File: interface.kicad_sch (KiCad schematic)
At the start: 10 parts, among them J6 JST Header, Q3 DTC043Z, Q5 DTC043Z, SW2 RotaryEncoder_Switch

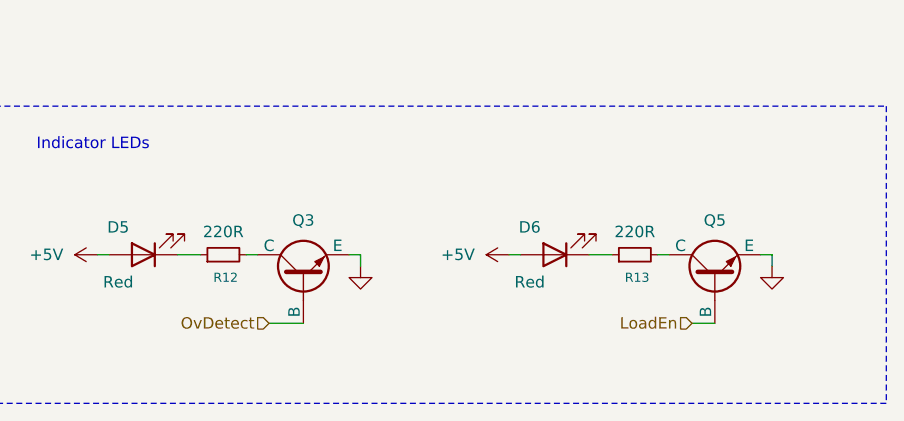
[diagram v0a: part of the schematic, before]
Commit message: Biased NPN transistor correct schematic symbol, Resistor values
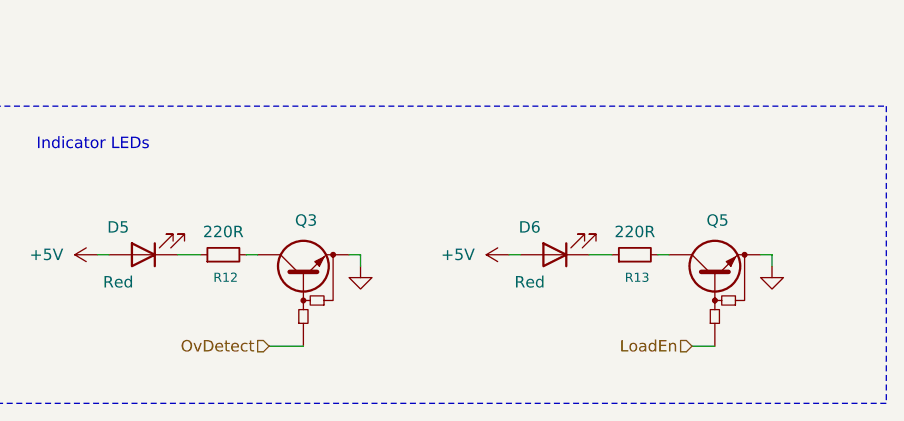
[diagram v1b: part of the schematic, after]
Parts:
- Q3, Q5: symbol Simulation_SPICE:NPN -> Device:Q_NPN_BRT
- R12, R13: footprint (none) -> Resistor_SMD:R_0805_2012Metric_Pad1.20x1.40mm_HandSolder; LCSC Part # (none) -> C844830
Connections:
- net GND: now also Q3.E, Q5.E; no longer Q3.3 (E), Q5.3 (E)
- net LoadEn: now also Q5.B; no longer Q5.2 (B)
- net OvDetect: now also Q3.B; no longer Q3.2 (B)
- net at R13.2: now also Q5.C; no longer Q5.1 (C)
- net at R12.2: now also Q3.C; no longer Q3.1 (C)
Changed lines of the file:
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@@
 	(wire
 		(pts
-			(xy 63.5 152.4) (xy 59.69 152.4)
-		)
-		(stroke
-			(width 0)
-			(type default)
-		)
-	)
-	(wire
-		(pts
-			(xy 109.22 152.4) (xy 106.68 152.4)
+			(xy 63.5 154.94) (xy 59.69 154.94)
+		)
+		(stroke
+			(width 0)
+			(type default)
+		)
+	)
+	(wire
+		(pts
+			(xy 109.22 154.94) (xy 106.68 154.94)
 		)
 		(stroke
@@
 	(hierarchical_label "LoadEn"
 		(shape input)
-		(at 106.68 152.4 180)
+		(at 106.68 154.94 180)
 		(effects
 			(font
@@
 	(hierarchical_label "OvDetect"
 		(shape input)
-		(at 59.69 152.4 180)
+		(at 59.69 154.94 180)
 		(effects
 			(font
@@
 			)
 		)
-		(property "Footprint" ""
+		(property "Footprint" "Resistor_SMD:R_0805_2012Metric_Pad1.20x1.40mm_HandSolder"
 			(at 100.33 144.78 0)
 			(effects
@@
 			)
 		)
-		(property "Datasheet" "~"
+		(property "Datasheet" "https://www.lcsc.com/datasheet/C844830.pdf"
 			(at 100.33 144.78 0)
 			(effects
@@
 			)
 		)
-		(property "Description" "Resistor, small symbol"
+		(property "Description" "VISHAY CRCW0805220RFKEA"
 			(at 100.33 144.78 0)
+			(effects
+				(font
+					(size 1.27 1.27)
+				)
+				(hide yes)
+			)
+		)
+		(property "LCSC Part #" "C844830"
+			(at 100.33 144.78 90)
 			(effects
 				(font
@@
 	)
 	(symbol
-		(lib_id "Simulation_SPICE:NPN")
-		(at 109.22 147.32 90)
+		(lib_id "Device:Q_NPN_BRT")
+		(at 109.22 146.05 90)
 		(unit 1)
 		(exclude_from_sim no)
@@
 		(fields_autoplaced yes)
 		(property "Reference" "Q5"
-			(at 109.22 140.97 90)
+			(at 109.5248 140.97 90)
 			(effects
 				(font
@@
 		)
 		(property "Value" "DTC043Z"
-			(at 109.22 140.97 90)
+			(at 109.22 139.7 90)
 			(effects
 				(font
@@
 		)
 		(property "Footprint" ""
-			(at 109.22 83.82 0)
+			(at 109.22 146.05 0)
 			(effects
 				(font
@@
 		)
 		(property "Datasheet" "https://www.lcsc.com/datasheet/C96459.pdf"
-			(at 109.22 83.82 0)
+			(at 109.22 82.55 0)
 			(effects
 				(font
@@
 		)
 		(property "Description" ""
-			(at 109.22 147.32 0)
-			(effects
-				(font
-					(size 1.27 1.27)
-				)
-				(hide yes)
-			)
-		)
-		(property "Sim.Device" "NPN"
-			(at 109.22 147.32 0)
-			(effects
-				(font
-					(size 1.27 1.27)
-				)
-				(hide yes)
-			)
-		)
-		(property "Sim.Type" "GUMMELPOON"
-			(at 109.22 147.32 0)
-			(effects
-				(font
-					(size 1.27 1.27)
-				)
-				(hide yes)
-			)
-		)
-		(property "Sim.Pins" "1=C 2=B 3=E"
-			(at 109.22 147.32 0)
+			(at 109.22 146.05 0)
 			(effects
 				(font
@@
 		)
 		(property "LCSC Part #" "C96459"
-			(at 109.22 147.32 90)
-			(effects
-				(font
-					(size 1.27 1.27)
-				)
-				(hide yes)
-			)
-		)
-		(pin "2"
-		)
-		(pin "3"
-		)
-		(pin "1"
+			(at 109.22 146.05 90)
+			(effects
+				(font
+					(size 1.27 1.27)
+				)
+				(hide yes)
+			)
+		)
+		(pin "B"
+		)
+		(pin "C"
+		)
+		(pin "E"
 		)
 		(instances
@@
 	)
 	(symbol
-		(lib_id "Simulation_SPICE:NPN")
-		(at 63.5 147.32 90)
+		(lib_id "Device:Q_NPN_BRT")
+		(at 63.5 146.05 90)
 		(unit 1)
 		(exclude_from_sim no)
@@
 		(fields_autoplaced yes)
 		(property "Reference" "Q3"
-			(at 63.5 140.97 90)
+			(at 63.8048 140.97 90)
 			(effects
 				(font
@@
 		)
 		(property "Value" "DTC043Z"
-			(at 63.5 140.97 90)
+			(at 63.5 139.7 90)
 			(effects
 				(font
@@
 		)
 		(property "Footprint" ""
-			(at 63.5 83.82 0)
+			(at 63.5 146.05 0)
 			(effects
 				(font
@@
 		)
 		(property "Datasheet" "https://www.lcsc.com/datasheet/C96459.pdf"
-			(at 63.5 83.82 0)
-			(effects
-				(font
-					(size 1.27 1.27)
-				)
-				(hide yes)
-			)
-		)
-		(property "Description" ""
-			(at 63.5 147.32 0)
-			(effects
-				(font
-					(size 1.27 1.27)
-				)
-				(hide yes)
-			)
-		)
-		(property "Sim.Device" "NPN"
-			(at 63.5 147.32 0)
-			(effects
-				(font
-					(size 1.27 1.27)
-				)
-				(hide yes)
-			)
-		)
-		(property "Sim.Type" "GUMMELPOON"
-			(at 63.5 147.32 0)
-			(effects
-				(font
-					(size 1.27 1.27)
-				)
-				(hide yes)
-			)
-		)
-		(property "Sim.Pins" "1=C 2=B 3=E"
-			(at 63.5 147.32 0)
+			(at 63.5 146.05 0)
+			(effects
+				(font
+					(size 1.27 1.27)
+				)
+				(hide yes)
+			)
+		)
+		(property "Description" "NPN bias resistor bipolar junction transistor"
+			(at 63.5 146.05 0)
 			(effects
 				(font
@@
 		)
 		(property "LCSC Part #" "C96459"
-			(at 63.5 147.32 90)
-			(effects
-				(font
-					(size 1.27 1.27)
-				)
-				(hide yes)
-			)
-		)
-		(pin "2"
-		)
-		(pin "3"
-		)
-		(pin "1"
+			(at 63.5 146.05 90)
+			(effects
+				(font
+					(size 1.27 1.27)
+				)
+				(hide yes)
+			)
+		)
+		(pin "B"
+		)
+		(pin "E"
+		)
+		(pin "C"
 		)
 		(instances
@@
 			)
 		)
-		(property "Footprint" ""
+		(property "Footprint" "Resistor_SMD:R_0805_2012Metric_Pad1.20x1.40mm_HandSolder"
 			(at 54.61 144.78 0)
 			(effects
@@
 			)
 		)
-		(property "Datasheet" "~"
+		(property "Datasheet" "https://www.lcsc.com/datasheet/C844830.pdf"
 			(at 54.61 144.78 0)
 			(effects
@@
 			)
 		)
-		(property "Description" "Resistor, small symbol"
+		(property "Description" "VISHAY CRCW0805220RFKEA"
 			(at 54.61 144.78 0)
 			(effects
 				(font
+					(size 1.27 1.27)
+				)
+				(hide yes)
+			)
+		)
+		(property "LCSC Part #" "C844830"
+			(at 54.61 144.78 90)
+			(effects
+				(font

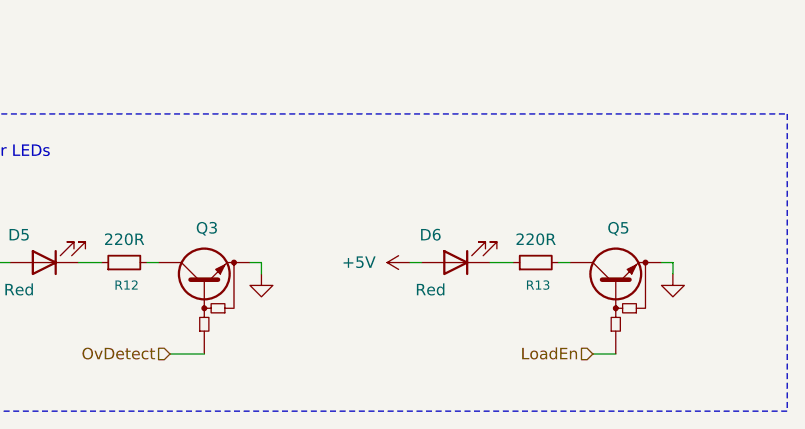
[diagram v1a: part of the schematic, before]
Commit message: 3D models added, mounting holes added
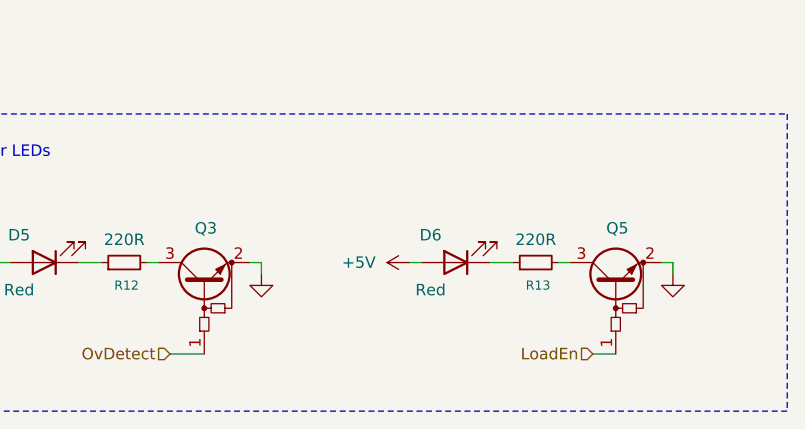
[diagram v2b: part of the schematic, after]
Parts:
- Q3, Q5: footprint (none) -> Package_TO_SOT_SMD:SOT-416; symbol Device:Q_NPN_BRT -> Transistor_BJT:Q_NPN_BRT_BEC
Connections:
- net GND: now also Q3.2 (E), Q5.2 (E); no longer Q3.E, Q5.E
- net LoadEn: now also Q5.1 (B); no longer Q5.B
- net OvDetect: now also Q3.1 (B); no longer Q3.B
- net at R13.2: now also Q5.3 (C); no longer Q5.C
- net at R12.2: now also Q3.3 (C); no longer Q3.C
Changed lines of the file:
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@@
 	)
 	(symbol
-		(lib_id "Device:Q_NPN_BRT")
+		(lib_id "Transistor_BJT:Q_NPN_BRT_BEC")
 		(at 109.22 146.05 90)
 		(unit 1)
@@
 		(fields_autoplaced yes)
 		(property "Reference" "Q5"
-			(at 109.5248 140.97 90)
+			(at 109.3978 140.97 90)
 			(effects
 				(font
@@
 			)
 		)
-		(property "Footprint" ""
+		(property "Footprint" "Package_TO_SOT_SMD:SOT-416"
 			(at 109.22 146.05 0)
 			(effects
@@
 			)
 		)
-		(pin "B"
-		)
-		(pin "C"
-		)
-		(pin "E"
+		(pin "1"
+		)
+		(pin "3"
+		)
+		(pin "2"
 		)
 		(instances
@@
 	)
 	(symbol
-		(lib_id "Device:Q_NPN_BRT")
+		(lib_id "Transistor_BJT:Q_NPN_BRT_BEC")
 		(at 63.5 146.05 90)
 		(unit 1)
@@
 		(fields_autoplaced yes)
 		(property "Reference" "Q3"
-			(at 63.8048 140.97 90)
+			(at 63.6778 140.97 90)
 			(effects
 				(font
@@
 			)
 		)
-		(property "Footprint" ""
+		(property "Footprint" "Package_TO_SOT_SMD:SOT-416"
 			(at 63.5 146.05 0)
 			(effects
@@
 			)
 		)
-		(pin "B"
-		)
-		(pin "E"
-		)
-		(pin "C"
+		(pin "1"
+		)
+		(pin "3"
+		)
+		(pin "2"
 		)
 		(instances

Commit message: Update digital transistor to more solderable by hand
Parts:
- Q3, Q5: value DTC043Z -> DTC043ZUBTL; footprint Package_TO_SOT_SMD:SOT-416 -> Package_TO_SOT_SMD:SOT-323_SC-70; LCSC Part # C96459 -> C962655
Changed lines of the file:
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@@
 			)
 		)
-		(property "Value" "DTC043Z"
+		(property "Value" "DTC043ZUBTL"
 			(at 109.22 139.7 90)
 			(effects
@@
 			)
 		)
-		(property "Footprint" "Package_TO_SOT_SMD:SOT-416"
+		(property "Footprint" "Package_TO_SOT_SMD:SOT-323_SC-70"
 			(at 109.22 146.05 0)
 			(effects
@@
 			)
 		)
-		(property "Description" ""
+		(property "Description" "NPN bias resistor bipolar junction transistor"
 			(at 109.22 146.05 0)
 			(effects
@@
 			)
 		)
-		(property "LCSC Part #" "C96459"
+		(property "LCSC Part #" "C962655"
 			(at 109.22 146.05 90)
 			(effects
@@
 			)
 		)
-		(property "Value" "DTC043Z"
+		(property "Value" "DTC043ZUBTL"
 			(at 63.5 139.7 90)
 			(effects
@@
 			)
 		)
-		(property "Footprint" "Package_TO_SOT_SMD:SOT-416"
+		(property "Footprint" "Package_TO_SOT_SMD:SOT-323_SC-70"
 			(at 63.5 146.05 0)
 			(effects
@@
 			)
 		)
-		(property "LCSC Part #" "C96459"
+		(property "LCSC Part #" "C962655"
 			(at 63.5 146.05 90)
 			(effects

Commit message: PCB Routing
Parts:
- added J3: JST Header, Connector_JST:JST_XH_B16B-XH-A_1x16_P2.50mm_Vertical, symbol Connector:Conn_01x16_Socket
- added J5, J8: Conn_01x08_Socket, Connector_JST:JST_XH_B8B-XH-A_1x08_P2.50mm_Vertical, symbol Connector:Conn_01x08_Socket
- J6: symbol Connector:Conn_01x18_Socket -> Connector:Conn_01x16_Socket
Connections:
- net +3.3V: now also J6.15 (Pin_15), J6.2 (Pin_2), J3.15 (Pin_15), J3.2 (Pin_2), J5.6 (Pin_6), J8.6 (Pin_6); no longer J6.18 (Pin_18)
- net D0: now also J6.7 (Pin_7), J3.7 (Pin_7); no longer J6.10 (Pin_10)
- net D1: now also J6.8 (Pin_8), J3.8 (Pin_8); no longer J6.11 (Pin_11)
- net D2: now also J6.9 (Pin_9), J3.9 (Pin_9); no longer J6.12 (Pin_12)
- net D3: now also J6.10 (Pin_10), J3.10 (Pin_10); no longer J6.13 (Pin_13)
- net D4: now also J6.11 (Pin_11), J3.11 (Pin_11); no longer J6.14 (Pin_14)
- net D5: now also J6.12 (Pin_12), J3.12 (Pin_12); no longer J6.15 (Pin_15)
- net D6: now also J6.13 (Pin_13), J3.13 (Pin_13); no longer J6.16 (Pin_16)
- net D7: now also J6.14 (Pin_14), J3.14 (Pin_14); no longer J6.17 (Pin_17)
- net E: now also J6.6 (Pin_6), J3.6 (Pin_6); no longer J6.9 (Pin_9)
- net EncA: now also J5.5 (Pin_5), J8.5 (Pin_5); no longer J6.3 (Pin_3)
- net EncB: now also J5.4 (Pin_4), J8.4 (Pin_4); no longer J6.2 (Pin_2)
- net EncSw: now also J5.1 (Pin_1), J8.1 (Pin_1); no longer J6.4 (Pin_4)
- net GND: now also J6.16 (Pin_16), J6.5 (Pin_5), J3.1 (Pin_1), J3.16 (Pin_16), J3.5 (Pin_5), J5.8 (Pin_8), J8.8 (Pin_8)
- net LoadEn: now also J5.2 (Pin_2), J8.2 (Pin_2); no longer J6.7 (Pin_7)
- net OvDetect: now also J5.3 (Pin_3), J8.3 (Pin_3); no longer J6.6 (Pin_6)
- net RS: now also J6.4 (Pin_4), J3.4 (Pin_4); no longer J6.8 (Pin_8)
- net V0: now reaches DS1.3 (VO), RV1.2
- net V0: now also J6.3 (Pin_3), J3.3 (Pin_3)
- no-connect marks 1 -> 2
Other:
- note added: "Mounting Holes"
- moved on the sheet: DS1, RV1
